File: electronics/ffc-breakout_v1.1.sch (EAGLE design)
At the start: 3 parts, among them X2 AMP_SFW16R-2STE1LF

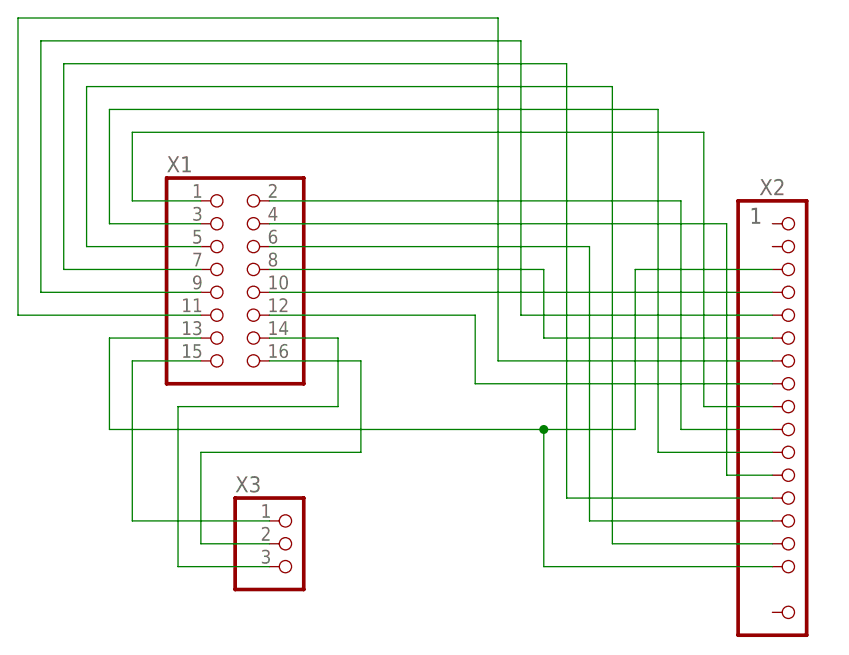
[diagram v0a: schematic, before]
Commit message: Electronics v1.1 draft updates
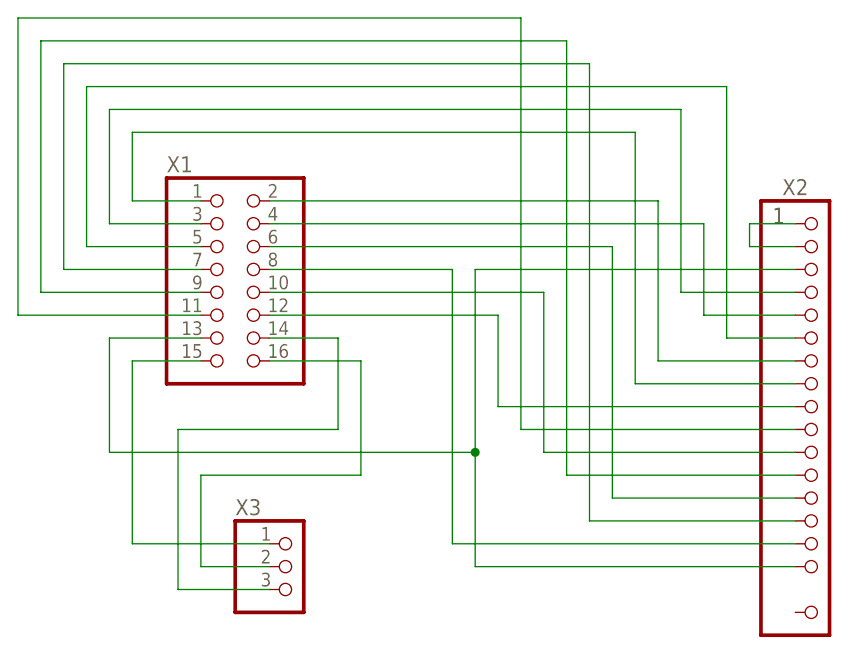
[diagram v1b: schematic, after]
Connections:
- removed net N$18: X1.12, X2.8
- new net N$5: X2.1, X2.2
- new net N$7: X1.2, X2.7
- net N$10: now also X1.5, X2.6; no longer X1.4, X2.12
- net N$11: now also X1.6, X2.13; no longer X1.5, X2.15
- net N$12: now also X1.7; no longer X1.6
- net N$13: now also X1.8, X2.15; no longer X1.7, X2.13
- net N$14: now also X1.9, X2.12; no longer X1.8, X2.6
- net N$15: now also X1.10, X2.11; no longer X1.9, X2.5
- net N$16: now also X1.11, X2.10; no longer X1.10, X2.4
- net N$17: now also X1.12, X2.9; no longer X1.11, X2.7
- net N$6: now also X2.8; no longer X2.9
- net N$8: now also X1.3, X2.4; no longer X1.2, X2.10
- net N$9: now also X1.4, X2.5; no longer X1.3, X2.11
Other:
- moved on the sheet: X2, X3
